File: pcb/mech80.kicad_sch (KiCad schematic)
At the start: 24 parts, among them J1 BM04B-SRSS, J2 Serial wire debug, SW1 MSK-12C02, SW2 PTS526-SK15, U1 AMS1117-3.3, U2 STM32F103C8T6, Y1 8MHz

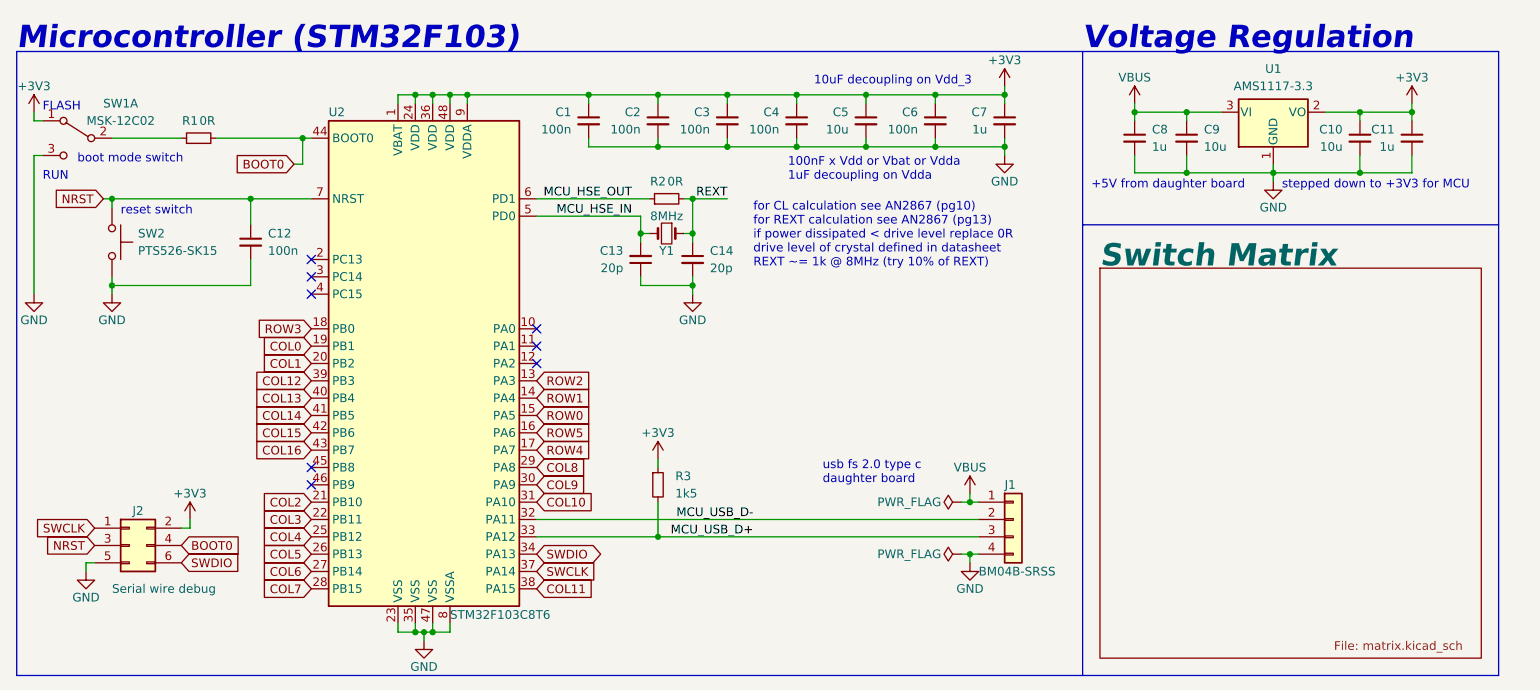
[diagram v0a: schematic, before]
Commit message: PCB has been wired completely and is ready for review before production
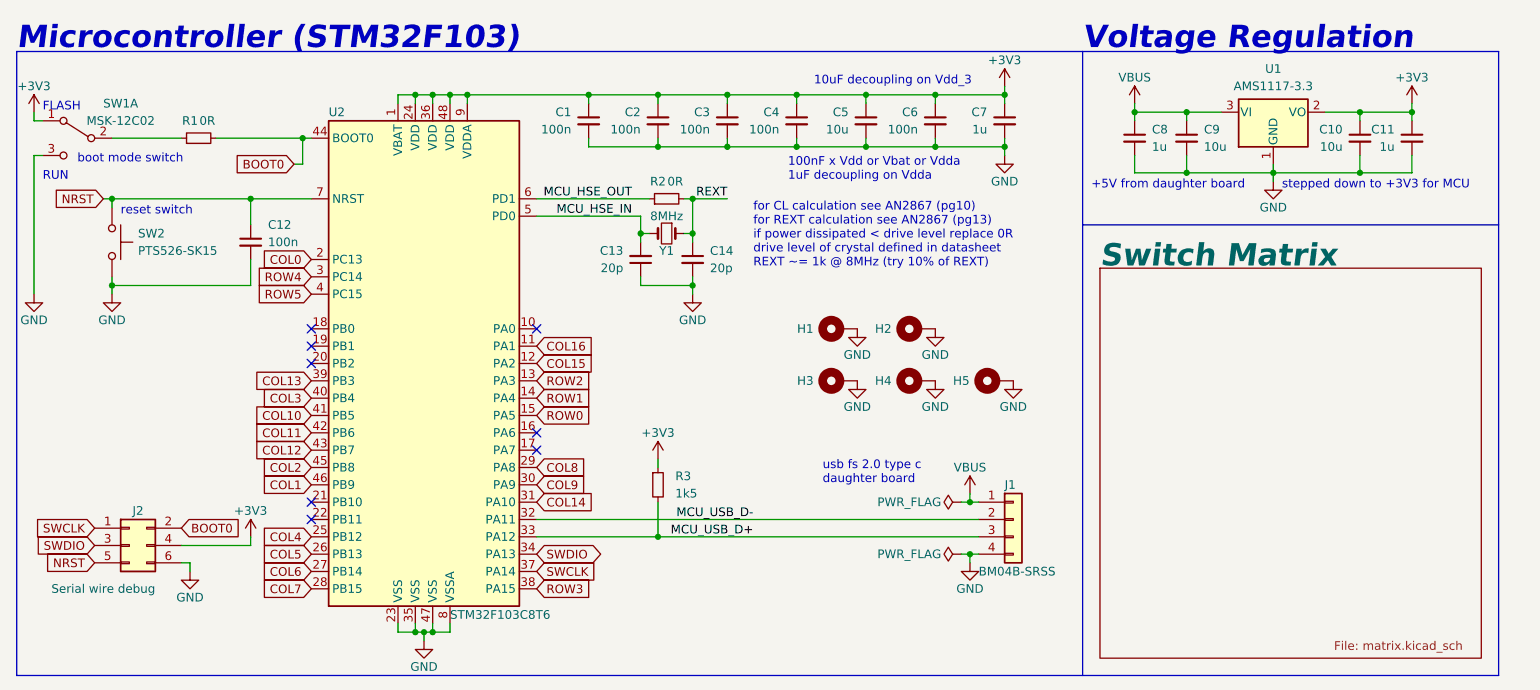
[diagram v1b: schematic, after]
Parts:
- added H1, H2, H3, H4, H5: MountingHole_Pad, MountingHole:MountingHole_3.2mm_M3_Pad, symbol Mechanical:MountingHole_Pad
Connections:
- net +3V3: now also J2.4 (Pin_4); no longer J2.2 (Pin_2)
- net BOOT0: now also J2.2 (Pin_2); no longer J2.4 (Pin_4)
- net COL0: now also U2.2 (PC13); no longer U2.19 (PB1)
- net COL1: now also U2.46 (PB9); no longer U2.20 (PB2)
- net COL10: now also U2.41 (PB5); no longer U2.31 (PA10)
- net COL11: now also U2.42 (PB6); no longer U2.38 (PA15)
- net COL12: now also U2.43 (PB7); no longer U2.39 (PB3)
- net COL13: now also U2.39 (PB3); no longer U2.40 (PB4)
- net COL14: now also U2.31 (PA10); no longer U2.41 (PB5)
- net COL15: now also U2.12 (PA2); no longer U2.42 (PB6)
- net COL16: now also U2.11 (PA1); no longer U2.43 (PB7)
- net COL2: now also U2.45 (PB8); no longer U2.21 (PB10)
- net COL3: now also U2.40 (PB4); no longer U2.22 (PB11)
- net GND: now also J2.6 (Pin_6), H1.1, H2.1, H3.1, H4.1, H5.1; no longer J2.5 (Pin_5)
- net NRST: now also J2.5 (Pin_5); no longer J2.3 (Pin_3)
- net ROW3: now also U2.38 (PA15); no longer U2.18 (PB0)
- net ROW4: now also U2.3 (PC14); no longer U2.17 (PA7)
- net ROW5: now also U2.4 (PC15); no longer U2.16 (PA6)
- net SWDIO: now also J2.3 (Pin_3); no longer J2.6 (Pin_6)
